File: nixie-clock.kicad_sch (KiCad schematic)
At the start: 84 parts, among them J1 Power Input, J2 ARGB, J3 I2C, J4 SWD, J5 ESP-Connector, Q1 FDS2734, SW1 PTS815, U1 TPS62175DQC, U2 USBLC6-2SC6, U3 STM32F103CBTx, U4 TC1185, U5 LT3757AEMSE, U6 Dot1, U7 Dot2, U8 SN74HCS541

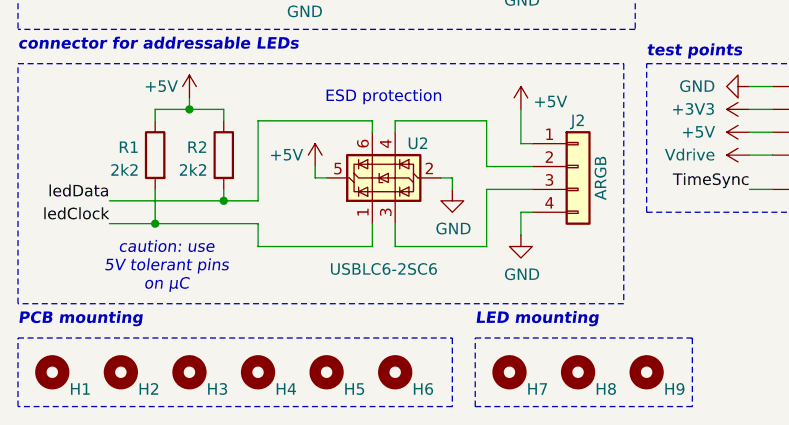
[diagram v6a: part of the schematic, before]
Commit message: Add note to ESD protection on ARGB connector
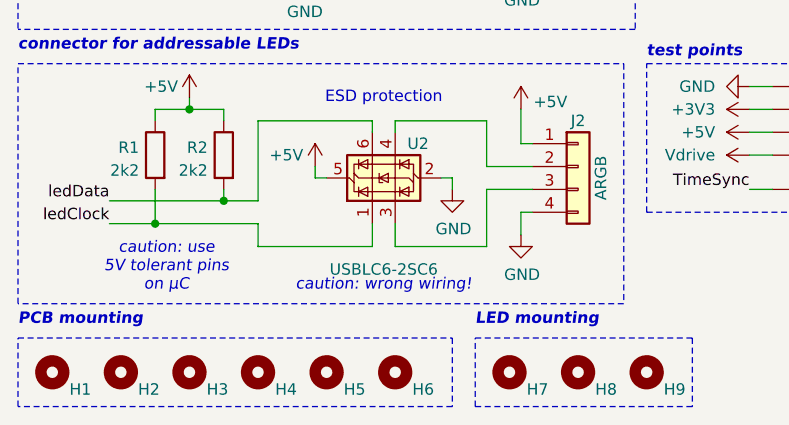
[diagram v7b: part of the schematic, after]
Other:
- note added: "caution: wrong wiring!"
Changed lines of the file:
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@@
+		)
+	)
+	(text "caution: wrong wiring!"
+		(exclude_from_sim no)
+		(at 54.61 270.51 0)
+		(effects
+			(font
+				(size 1.27 1.27)
+				(italic yes)
+			)
+			(justify bottom)
 		)
 	)
